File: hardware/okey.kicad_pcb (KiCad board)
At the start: 2 copper layers, 34 parts, among them IC1 4094N, IC2 4094N, P1 ROW_JMP, P2 CONN_02X13, P3 CONN_02X03, P4 CONN_02X08, P5 CONN_02X03, P6 CONN_02X10, SW1 MX_D, SW10 MX_D, SW11 MX_D, SW12 MX_D, SW13 MX_D, SW2 MX_D, SW3 MX_D, SW4 MX_D, SW5 MX_D, SW6 MX_D, SW7 MX_D, SW8 MX_D, SW9 MX_D, U1 4053, U2 4024

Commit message: ... PCB layout: all lines connected ...
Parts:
- moved P3 1.27 mm to (180.3, 19.1)
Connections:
- P3 pad 1: Net-(IC1-Pad2) -> Net-(P3-Pad1)
- P3 pad 3: Net-(P3-Pad3) -> Net-(IC1-Pad2)
- P5 pad 1: Net-(IC1-Pad2) -> Net-(P3-Pad1)
- P5 pad 3: Net-(P3-Pad3) -> Net-(IC1-Pad2)
- U2 pad 2: Net-(P3-Pad3) -> Net-(P3-Pad1)
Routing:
- net Net-(P3-Pad3): track 174.4 -> 0.00 mm
- net Net-(P3-Pad1): track 0.00 -> 120.0 mm, vias 0 -> 2
- net GND: track 192.7 -> 308.6 mm, vias 0 -> 8
- net VDD: track 614.3 -> 591.0 mm
- net Net-(IC1-Pad1): track 290.3 -> 277.4 mm
- net Net-(IC1-Pad3): track 242.1 -> 231.1 mm
- net Net-(IC1-Pad2): track 104.1 -> 98.4 mm
- net Net-(D8-Pad1): track 113.2 -> 111.6 mm
- net Net-(P3-Pad4): track 35.6 -> 34.4 mm
- net Net-(P5-Pad4): track 39.2 -> 38.4 mm

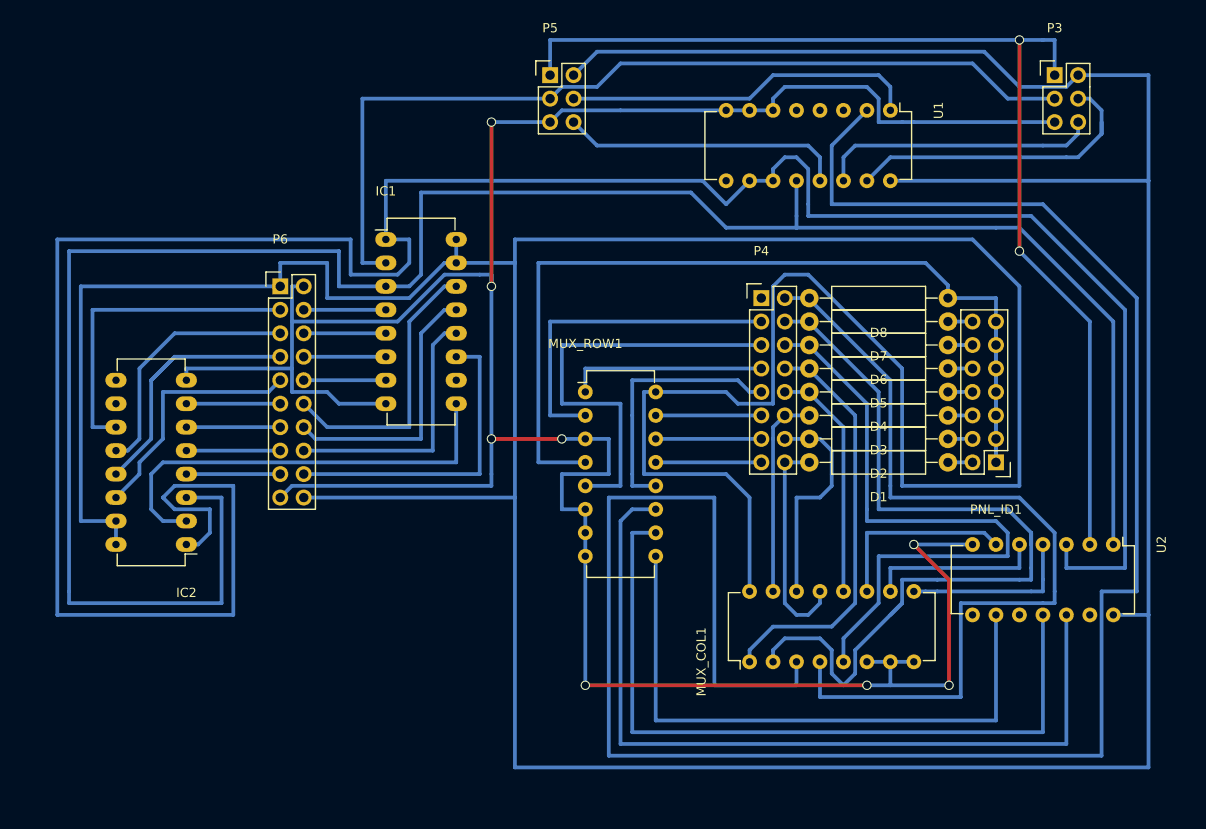
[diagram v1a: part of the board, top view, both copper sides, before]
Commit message: ... PCB layout: reducing pcb width ...
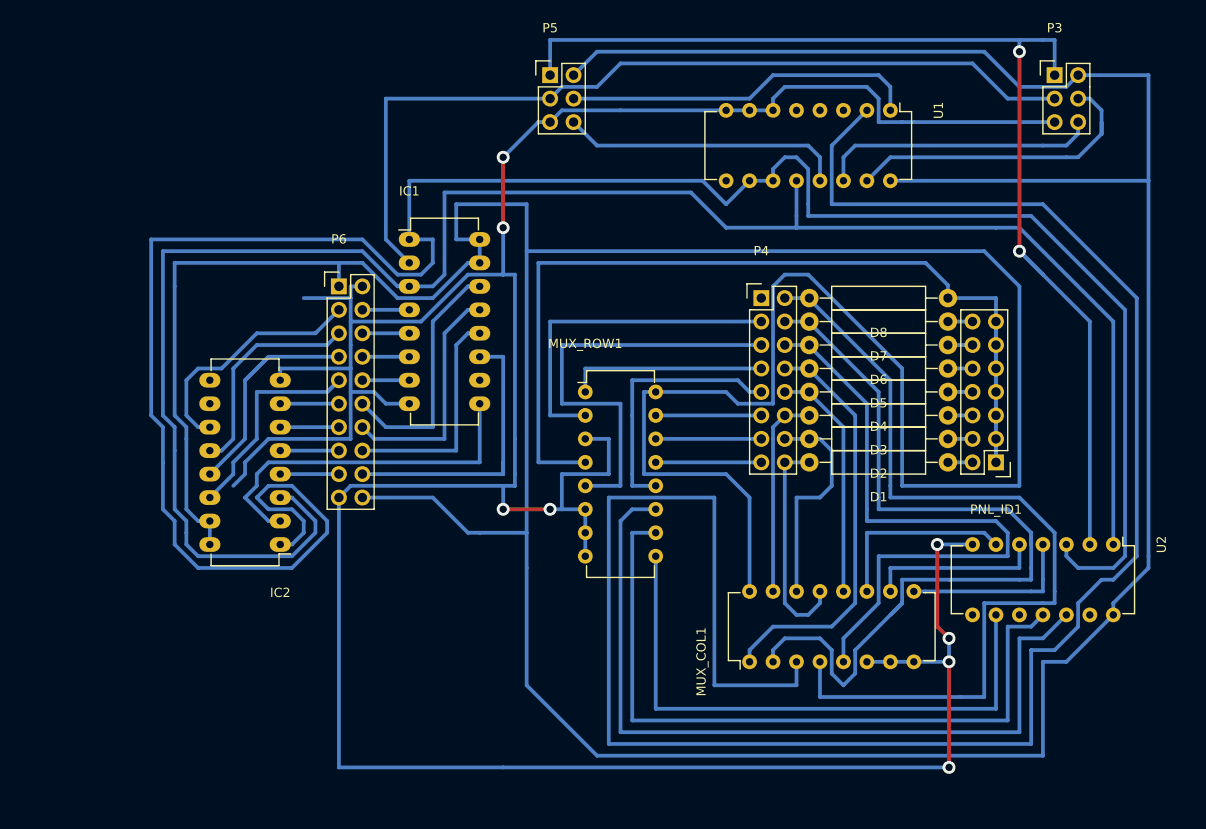
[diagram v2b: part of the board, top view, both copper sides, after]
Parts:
- moved IC2 10.2 mm to (96.5, 69.8)
- moved P6 6.35 mm to (102.9, 41.9)
- moved IC1 2.54 mm to (110.5, 36.8)
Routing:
- net GND: track 308.6 -> 360.2 mm
- net Net-(IC1-Pad1): track 277.4 -> 245.2 mm
- net Net-(IC1-Pad3): track 231.1 -> 203.3 mm
- net VDD: track 591.0 -> 571.0 mm
- net Net-(IC1-Pad9): track 48.0 -> 38.9 mm
- net Net-(IC2-Pad11): track 35.6 -> 26.5 mm
- net Net-(MUX_COL1-Pad3): track 226.8 -> 219.8 mm
- net Net-(IC1-Pad2): track 98.4 -> 94.4 mm
- net Net-(MUX_ROW1-Pad11): track 90.7 -> 86.7 mm
- net Net-(IC2-Pad12): track 27.5 -> 23.7 mm
- net Net-(IC1-Pad7): track 8.89 -> 5.08 mm
- net Net-(IC1-Pad6): track 8.89 -> 5.08 mm
- net Net-(IC1-Pad5): track 8.89 -> 5.08 mm
- net Net-(IC1-Pad4): track 8.89 -> 5.08 mm
- net Net-(IC2-Pad13): track 30.4 -> 26.5 mm
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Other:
- net class Default: via_dia 1.016 -> 1.397

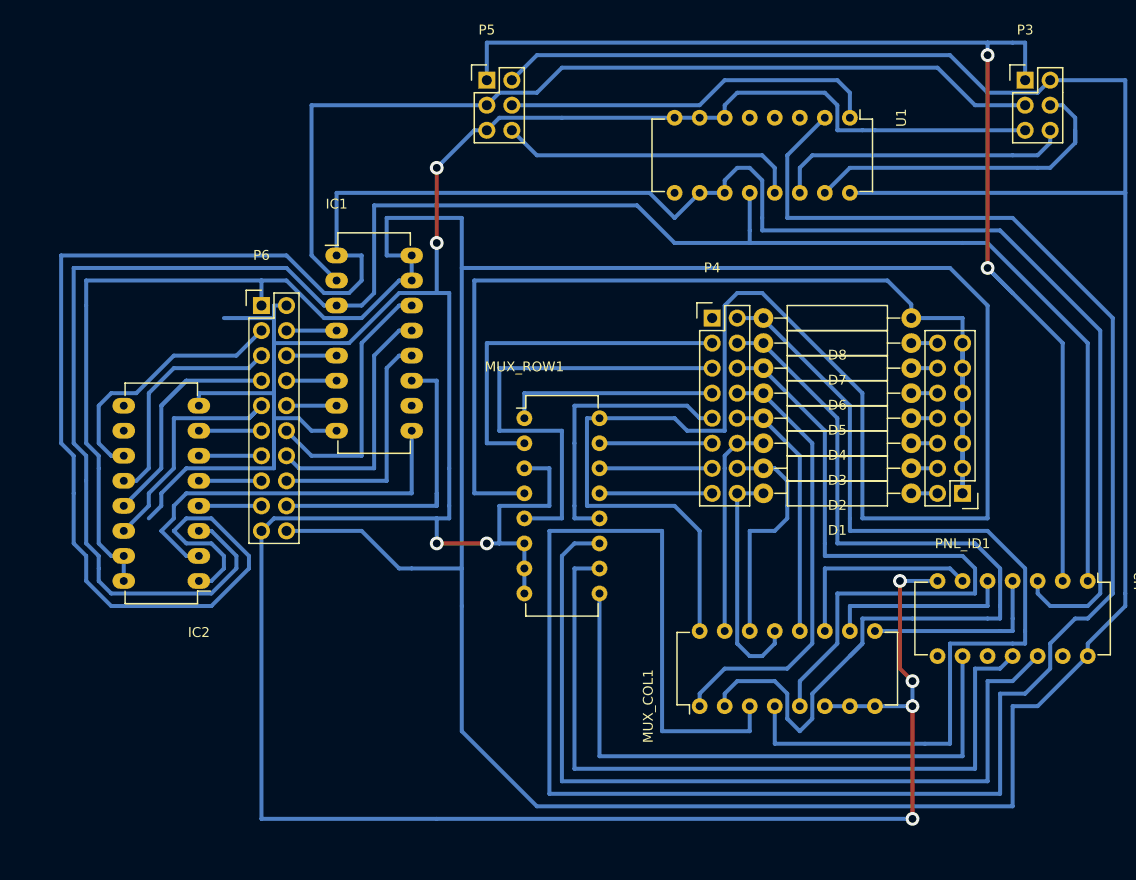
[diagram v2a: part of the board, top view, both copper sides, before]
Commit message: ... PCB layout: reducing pcb width ...
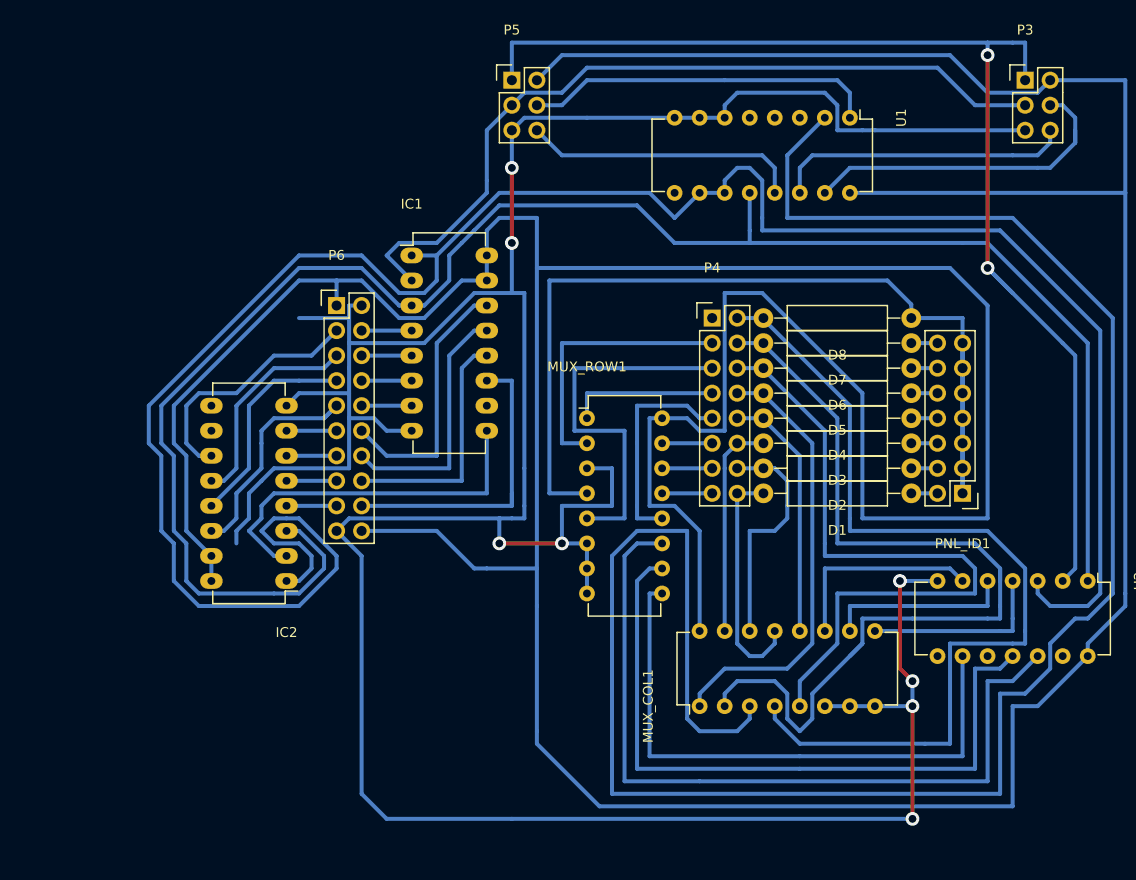
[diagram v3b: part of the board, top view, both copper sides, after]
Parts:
- moved IC2 8.89 mm to (105.4, 69.8)
- moved IC1 7.62 mm to (118.1, 36.8)
- moved P6 7.62 mm to (110.5, 41.9)
- moved MUX_ROW1 6.35 mm to (135.9, 53.3)
- moved P5 2.54 mm to (128.3, 19.1)
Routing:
- net VDD: track 571.0 -> 526.8 mm
- net Net-(IC1-Pad1): track 245.2 -> 221.1 mm
- net Net-(IC1-Pad3): track 203.3 -> 182.5 mm
- net Net-(MUX_COL1-Pad3): track 219.8 -> 204.1 mm
- net GND: track 360.2 -> 346.0 mm
- net Net-(IC1-Pad2): track 94.4 -> 81.6 mm
- net Net-(D8-Pad1): track 111.6 -> 102.7 mm
- net Net-(MUX_ROW1-Pad5): track 47.0 -> 38.1 mm
- net Net-(MUX_ROW1-Pad2): track 36.8 -> 27.9 mm
- net Net-(MUX_ROW1-Pad10): track 78.0 -> 70.9 mm
- net Net-(MUX_ROW1-Pad15): track 11.4 -> 5.08 mm
- net Net-(MUX_ROW1-Pad14): track 11.4 -> 5.08 mm
- net Net-(MUX_ROW1-Pad13): track 11.4 -> 5.08 mm
- net Net-(MUX_ROW1-Pad12): track 28.5 -> 22.1 mm
- net Net-(MUX_ROW1-Pad1): track 21.6 -> 15.2 mm
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
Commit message: ... PCB: shrink SPI board, add filled zones, connect key switch row ...
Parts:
- moved P5 5.39 mm to (132.1, 22.9)
- moved U2 3.81 mm to (182.9, 69.8)
- moved P3 3.81 mm to (180.3, 22.9)
- moved U1 2.54 mm to (162.6, 25.4)
- moved MUX_COL1 2.54 mm to (144.8, 82.5)
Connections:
- net Net-(P1-Pad10) renamed /Cherry-MX Switches Row 3x/ROW
- U1 pad 9: (no net) -> Net-(IC1-Pad1)
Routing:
- net /Cherry-MX Switches Row 3x/ROW: track 0.00 -> 663.4 mm
- net Net-(P2-Pad25): track 0.00 -> 103.0 mm
- net Net-(P2-Pad1): track 0.00 -> 97.3 mm
- net Net-(P2-Pad23): track 0.00 -> 87.7 mm
- net Net-(P2-Pad3): track 0.00 -> 82.0 mm
- net Net-(P2-Pad21): track 0.00 -> 72.5 mm
- net Net-(P2-Pad5): track 0.00 -> 66.8 mm
- net Net-(P2-Pad19): track 0.00 -> 56.6 mm
- net Net-(P2-Pad7): track 0.00 -> 50.8 mm
- net Net-(P2-Pad17): track 0.00 -> 40.6 mm
- net Net-(P2-Pad9): track 0.00 -> 34.9 mm
- net VDD: track 526.8 -> 499.6 mm
- net Net-(P2-Pad15): track 0.00 -> 26.5 mm
- net Net-(P3-Pad1): track 122.1 -> 100.7 mm
- net Net-(P2-Pad11): track 0.00 -> 20.8 mm
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- added copper zone on B.Cu, net /Cherry-MX Switches Row 3x/ROW
- added copper zone on B.Cu, net GND

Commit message: ... main PCB
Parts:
- moved P3 12.7 mm to (167.6, 22.9)
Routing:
- net GND: track 342.8 -> 330.1 mm
- net Net-(IC1-Pad2): track 79.2 -> 66.5 mm
- net Net-(P3-Pad6): track 28.6 -> 15.9 mm
- net Net-(P3-Pad4): track 32.4 -> 19.7 mm
- net VDD: track 499.6 -> 504.5 mm
- net Net-(P3-Pad1): track 100.7 -> 102.0 mm
- net Net-(P5-Pad4): track 31.5 -> 30.8 mm
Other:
- board outline added: 102.9 x 82.6 mm

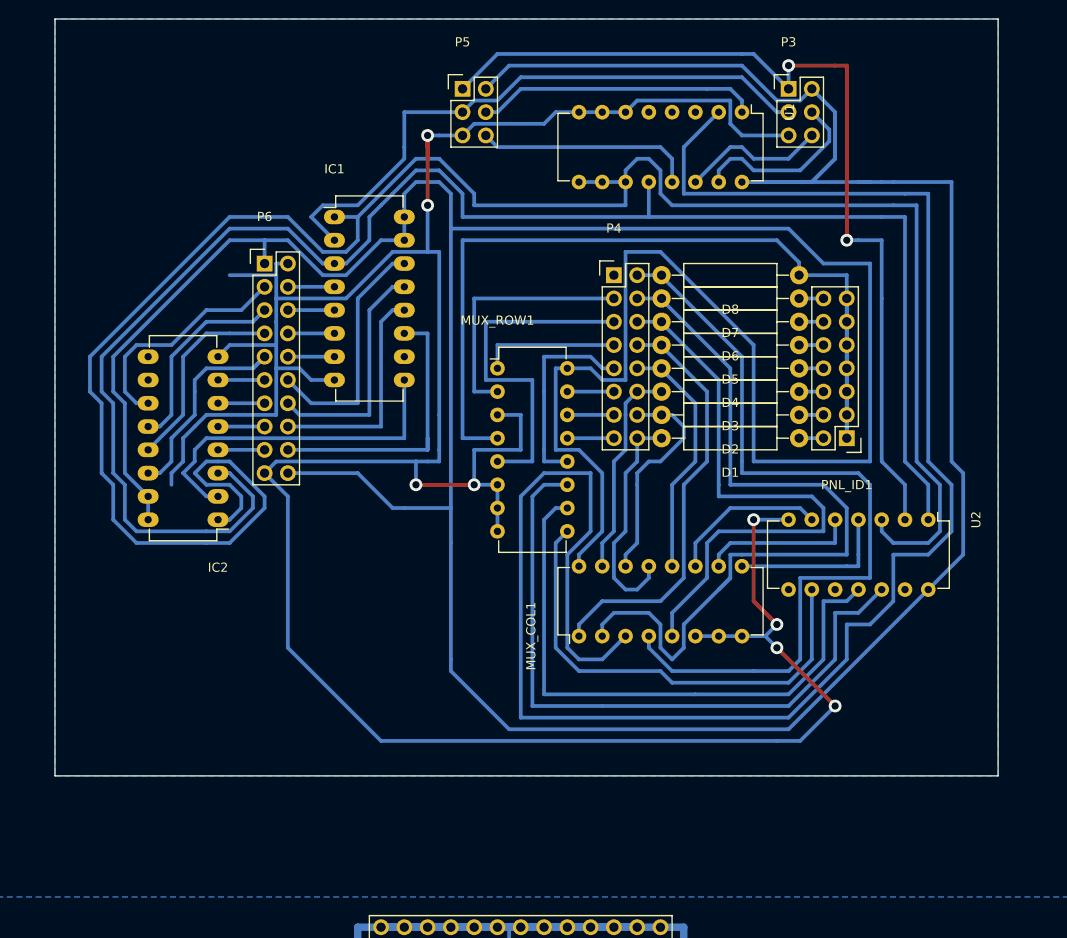
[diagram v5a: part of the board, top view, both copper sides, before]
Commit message: fix wrong connetion between counter bits and row/col multiplexer
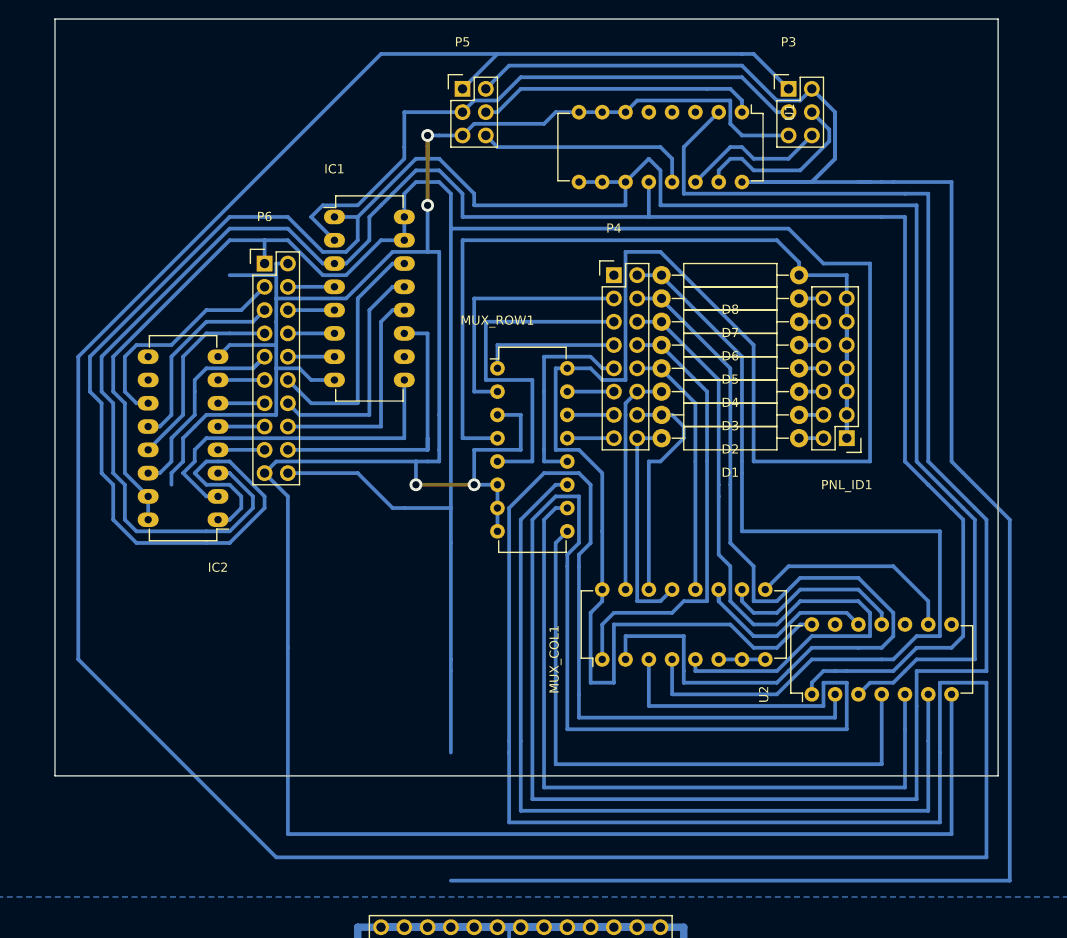
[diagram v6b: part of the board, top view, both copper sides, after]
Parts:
- moved U2 22.9 mm to (170.2, 88.9), turned to 90 degrees
- moved MUX_COL1 3.59 mm to (147.3, 85.1)
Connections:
- net /Cherry-MX Switches Row 3x/ROW renamed /Cherry-MX Switches Row 3x up to 8x /ROW
- U2 pad 11: Net-(MUX_ROW1-Pad10) -> Net-(MUX_COL1-Pad10)
- U2 pad 12: Net-(MUX_ROW1-Pad11) -> Net-(MUX_COL1-Pad11)
- U2 pad 4: Net-(MUX_COL1-Pad9) -> Net-(MUX_ROW1-Pad9)
- U2 pad 5: Net-(MUX_COL1-Pad10) -> Net-(MUX_ROW1-Pad10)
- U2 pad 6: Net-(MUX_COL1-Pad11) -> Net-(MUX_ROW1-Pad11)
- U2 pad 9: Net-(MUX_ROW1-Pad9) -> Net-(MUX_COL1-Pad9)
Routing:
- net Net-(P3-Pad1): track 102.0 -> 427.2 mm, vias 2 -> 0
- net Net-(MUX_COL1-Pad3): track 196.5 -> 282.6 mm
- net VDD: track 504.5 -> 590.4 mm
- net Net-(IC1-Pad3): track 182.7 -> 216.8 mm
- net Net-(MUX_ROW1-Pad11): track 73.5 -> 95.6 mm
- net Net-(IC1-Pad1): track 226.9 -> 248.0 mm
- net Net-(MUX_ROW1-Pad9): track 51.4 -> 69.1 mm
- net Net-(MUX_ROW1-Pad10): track 64.9 -> 81.8 mm
- net Net-(D6-Pad2): track 63.8 -> 78.6 mm
- net Net-(D8-Pad2): track 88.4 -> 102.9 mm
- net Net-(D7-Pad2): track 86.5 -> 99.2 mm
- net GND: track 330.1 -> 341.2 mm, vias 8 -> 4
- net Net-(MUX_COL1-Pad9): track 17.8 -> 23.0 mm
- net Net-(MUX_COL1-Pad11): track 17.3 -> 20.9 mm
- net Net-(MUX_COL1-Pad10): track 17.0 -> 20.4 mm
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- added copper zone on B.Cu, net /Cherry-MX Switches Row 3x/ROW
- removed copper zone on B.Cu, net /Cherry-MX Switches Row 3x up to 8x /ROW
- removed copper zone on B.Cu, net GND
